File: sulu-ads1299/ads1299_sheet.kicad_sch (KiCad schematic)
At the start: 15 parts, among them J8 through_hole, U4 ADS1299_TQFP-64

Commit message: Updated sulu-ads1299 rev2 layout and schematic
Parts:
- renumbered C8 to C13, C9 to C14, C10 to C15, C11 to C16, C12 to C17, C13 to C18, C14 to C19, C15 to C20, C16 to C21, C17 to C22, C18 to C23, C19 to C24, C20 to C25, J8 to J5

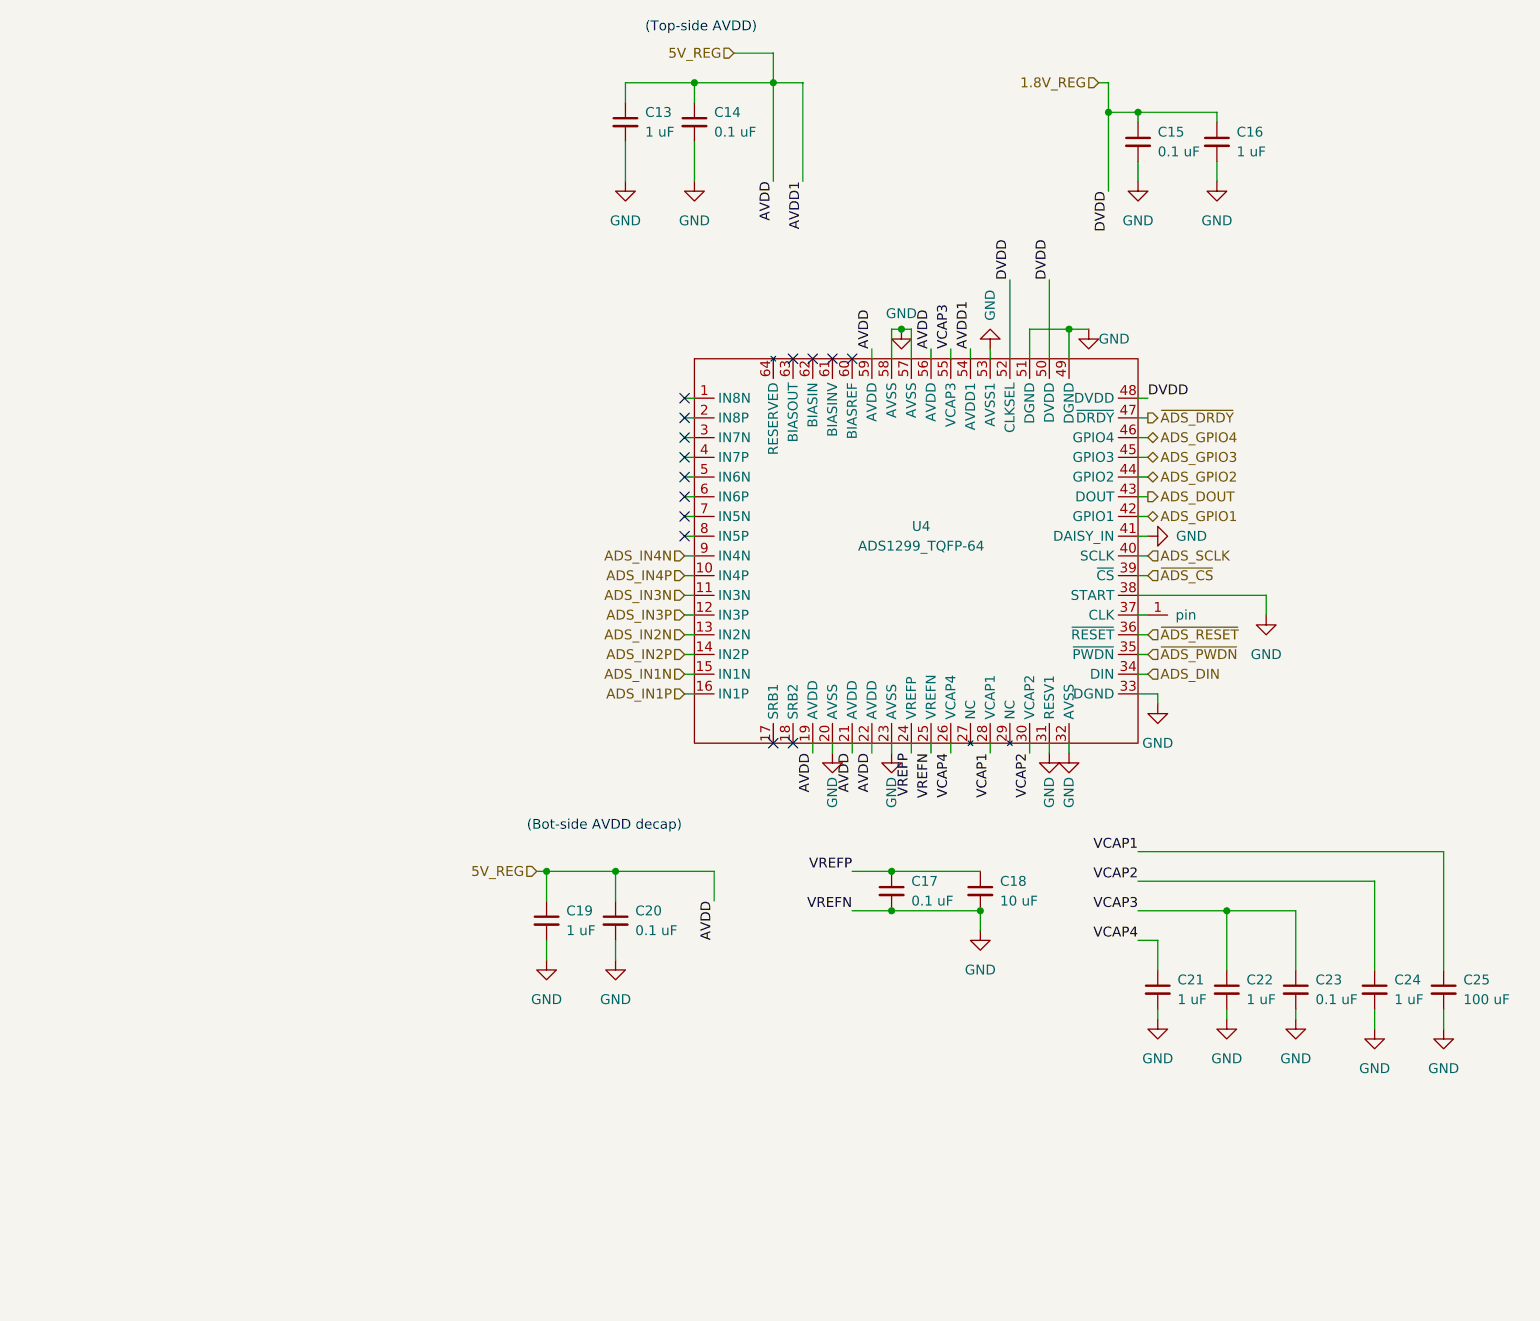
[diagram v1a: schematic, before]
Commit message: Sulu-ADS1299 components placed, new antenna, some routing
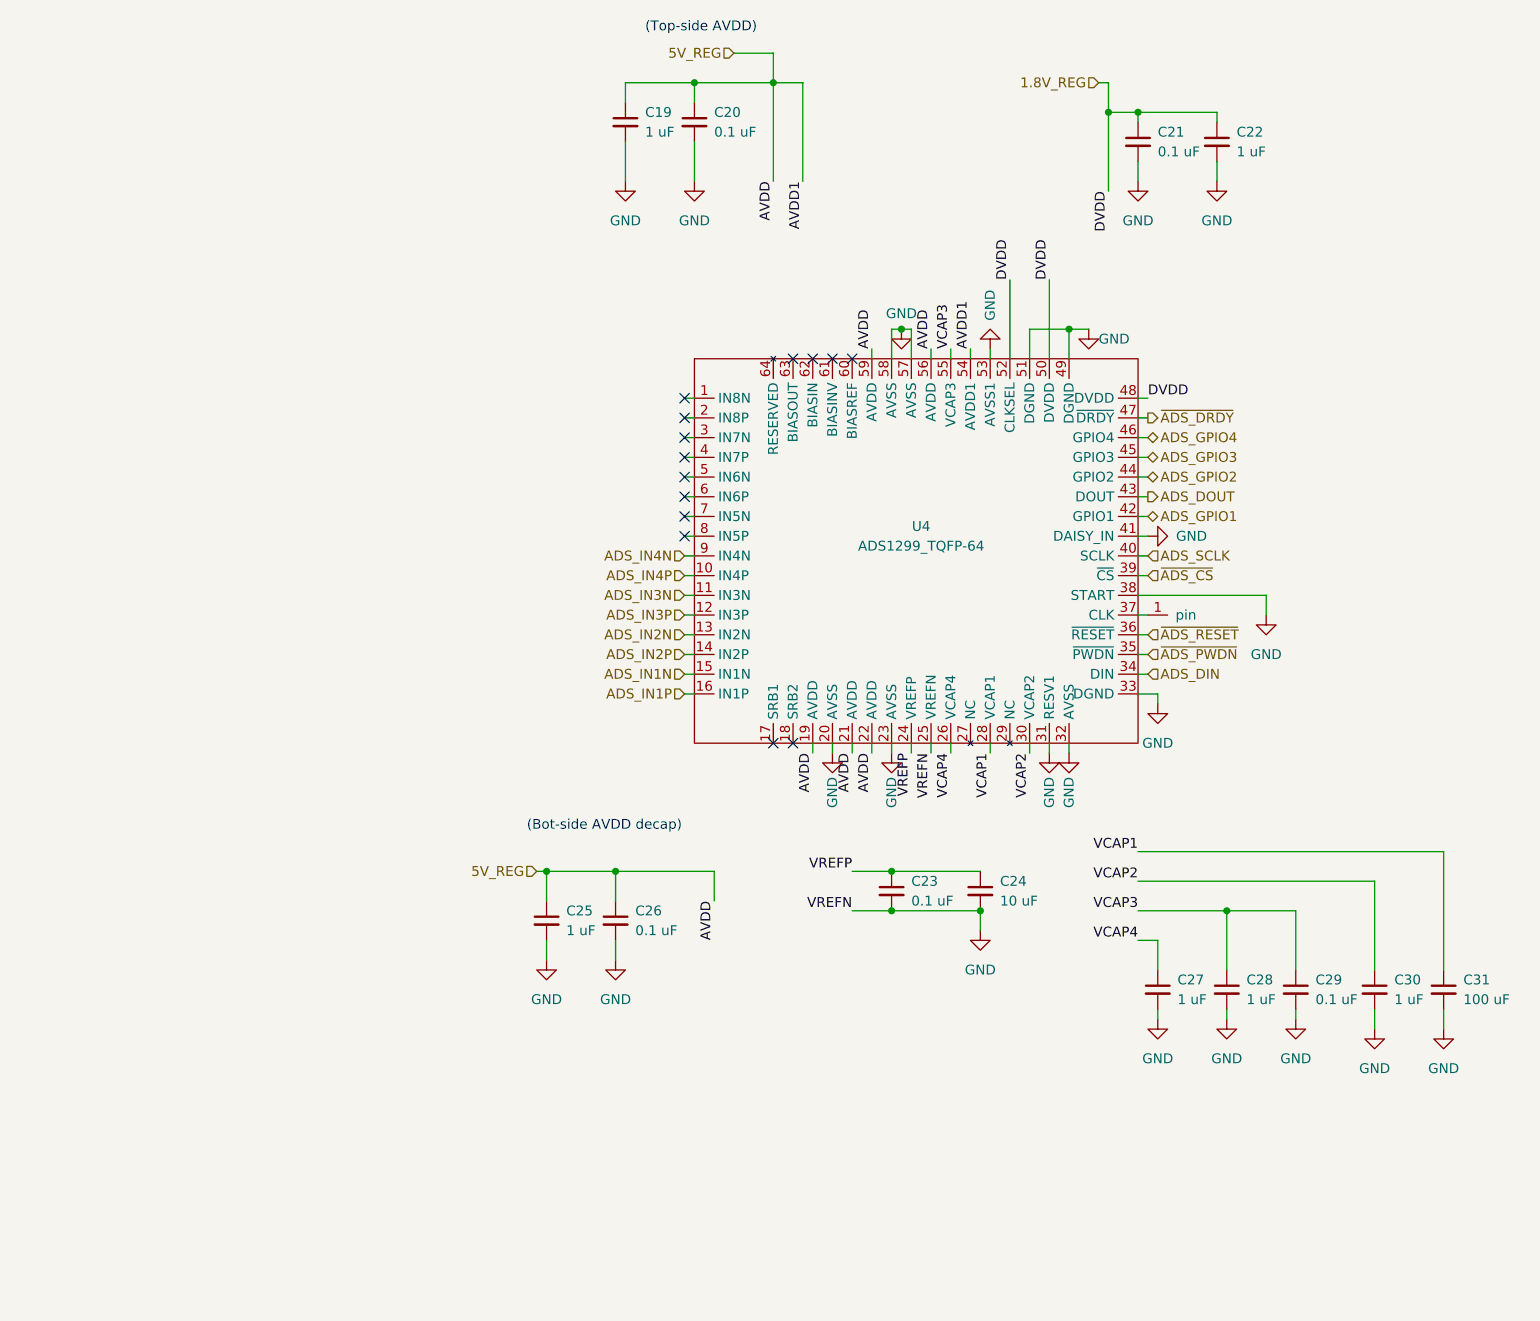
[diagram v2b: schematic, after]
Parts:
- renumbered C13 to C19, C14 to C20, C15 to C21, C16 to C22, C17 to C23, C18 to C24, C19 to C25, C20 to C26, C21 to C27, C22 to C28, C23 to C29, C24 to C30, C25 to C31

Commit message: Silkscreen cleaned, reduced TP footprint #, post design review
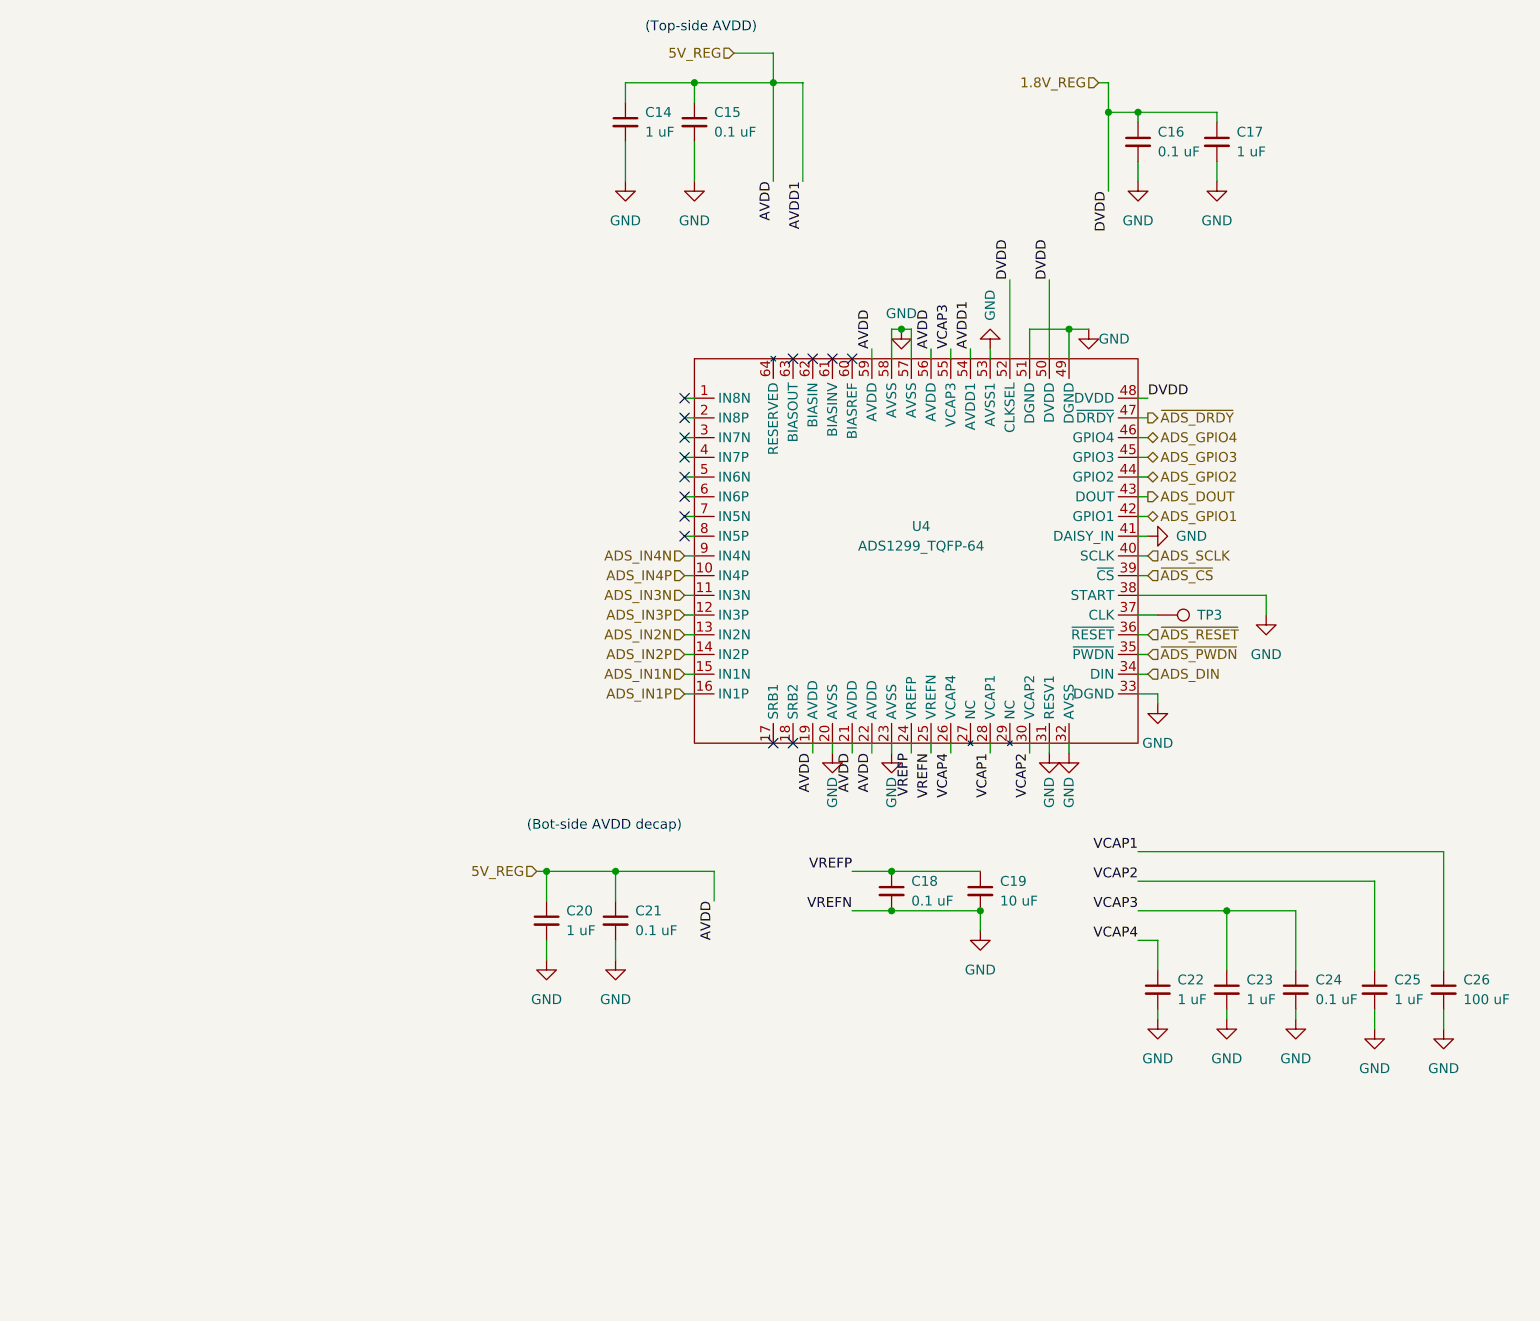
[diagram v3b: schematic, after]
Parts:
- removed J5: through_hole, SCUM:through_hole, symbol draft1library:through_hole
- added TP3: TestPoint, SCUM:through_hole, symbol Connector:TestPoint
- renumbered C19 to C14, C20 to C15, C21 to C16, C22 to C17, C23 to C18, C24 to C19, C25 to C20, C26 to C21, C27 to C22, C28 to C23, C29 to C24, C30 to C25, C31 to C26
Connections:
- net at U4.37 (CLK): now also TP3.1

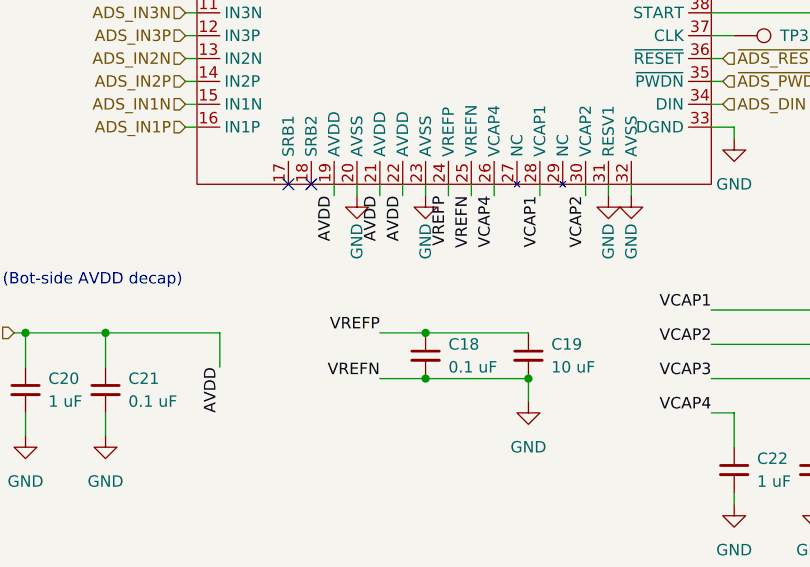
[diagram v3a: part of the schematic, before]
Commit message: BOM adjustments, protection Zener diodes, JLCPCB fab files
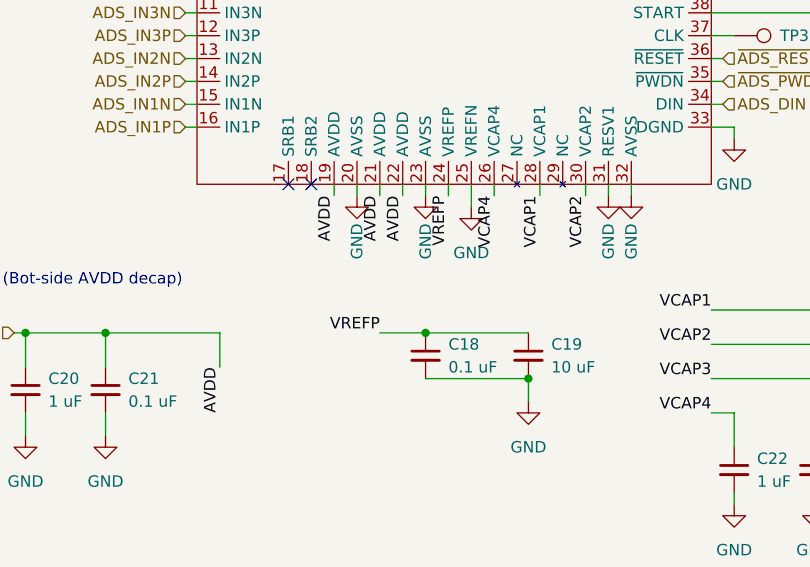
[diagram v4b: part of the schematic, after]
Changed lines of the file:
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@@
   (junction (at 152.4 134.62) (diameter 0) (color 0 0 0 0)
-  )
-  (junction (at 140.97 134.62) (diameter 0) (color 0 0 0 0)
   )
   (junction (at 168.91 31.75) (diameter 0) (color 0 0 0 0)
@@
     (stroke (width 0) (type default) (color 0 0 0 0))
   )
+  (wire (pts (xy 146.05 113.03) (xy 146.05 115.57))
+    (stroke (width 0) (type default) (color 0 0 0 0))
+  )
   (wire (pts (xy 172.72 86.36) (xy 173.99 86.36))
     (stroke (width 0) (type default) (color 0 0 0 0))
@@
     (stroke (width 0) (type default) (color 0 0 0 0))
   )
-  (wire (pts (xy 135.89 134.62) (xy 140.97 134.62))
-    (stroke (width 0) (type default) (color 0 0 0 0))
-  )
   (wire (pts (xy 115.57 27.94) (xy 106.68 27.94))
     (stroke (width 0) (type default) (color 0 0 0 0))
@@
     (stroke (width 0) (type default) (color 0 0 0 0))
   )
-  (wire (pts (xy 146.05 113.03) (xy 146.05 114.3))
-    (stroke (width 0) (type default) (color 0 0 0 0))
-  )
   (wire (pts (xy 96.52 138.43) (xy 96.52 140.97))
     (stroke (width 0) (type default) (color 0 0 0 0))
@@
     (effects (font (size 1.27 1.27)) (justify right bottom))
   )
-  (label "VREFN" (at 146.05 114.3 270)
-    (effects (font (size 1.27 1.27)) (justify right bottom))
-  )
   (label "AVDD" (at 138.43 114.3 270)
-    (effects (font (size 1.27 1.27)) (justify right bottom))
-  )
-  (label "VREFN" (at 135.89 134.62 180)
     (effects (font (size 1.27 1.27)) (justify right bottom))
   )
@@
       (effects (font (size 1.27 1.27)) hide)
     )
+    (pin "1")
+  )
+  (symbol (lib_id "power:GND") (at 146.05 115.57 0) (unit 1)
+    (in_bom yes) (on_board yes) (fields_autoplaced)
+    (property "Reference" "#PWR0114" (id 0) (at 146.05 121.92 0)
+      (effects (font (size 1.27 1.27)) hide)
+    )
+    (property "Value" "GND" (id 1) (at 146.05 120.65 0))
+    (property "Footprint" "" (id 2) (at 146.05 115.57 0)
+      (effects (font (size 1.27 1.27)) hide)
+    )
+    (property "Datasheet" "" (id 3) (at 146.05 115.57 0)
+      (effects (font (size 1.27 1.27)) hide)
+    )

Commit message: DRC clean layout of Rev. 3
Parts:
- added C32: 0.01uF, Capacitor_SMD:C_0603_1608Metric, symbol Device:C_Small
- added R15: 4.99K, Resistor_SMD:R_0603_1608Metric, symbol Device:R_Small_US
- added R16: 392K, Resistor_SMD:R_0603_1608Metric, symbol Device:R_Small_US
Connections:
- net BIASINV: now reaches U4.61 (BIASINV)
- net BIASINV: now also C32.1, R16.1
- net BIASOUT: now reaches U4.63 (BIASOUT)
- net BIASOUT: now also C32.2, R15.2, R16.2
- new net ADS_BIAS: R15.1
- no-connect marks 14 -> 12
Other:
- note added: "Bias Electrode"
- moved on the sheet: C18, C19, C20, C21, C22, C23, C24, C25, C26
